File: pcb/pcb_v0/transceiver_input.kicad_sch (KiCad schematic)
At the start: 26 parts, among them U2 LM324

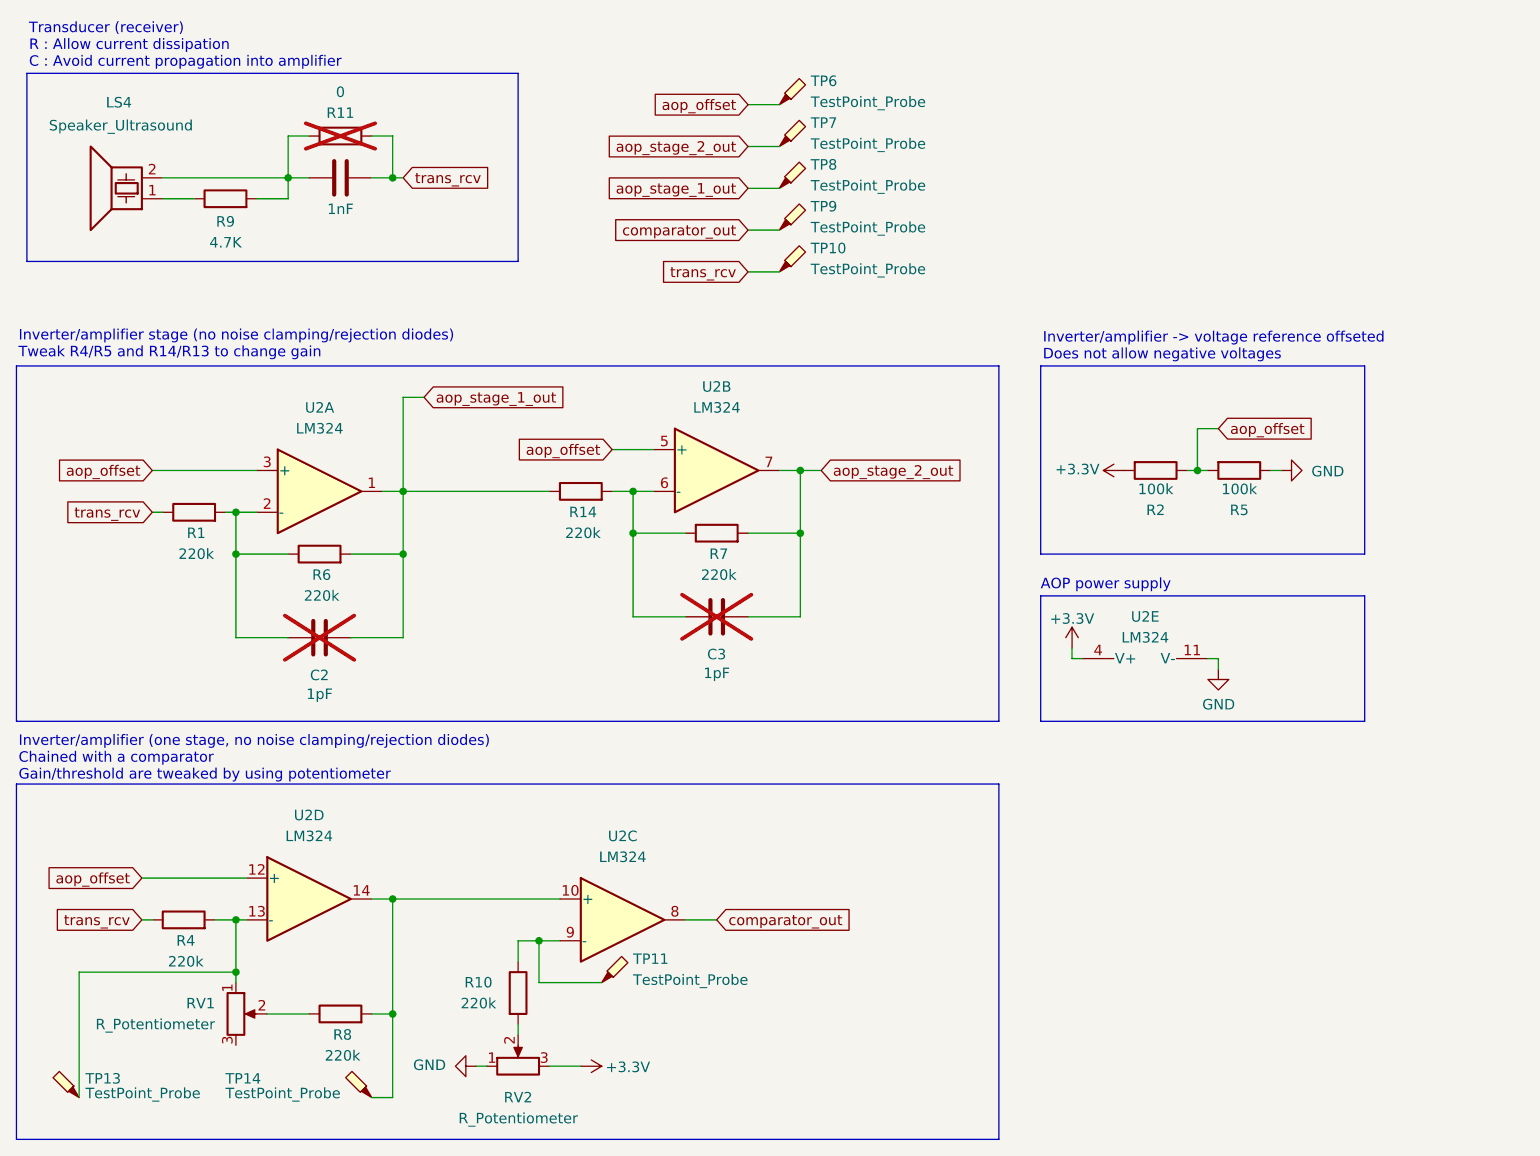
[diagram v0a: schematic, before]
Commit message: fix(pcb_v0): Update resistor and capacitor values
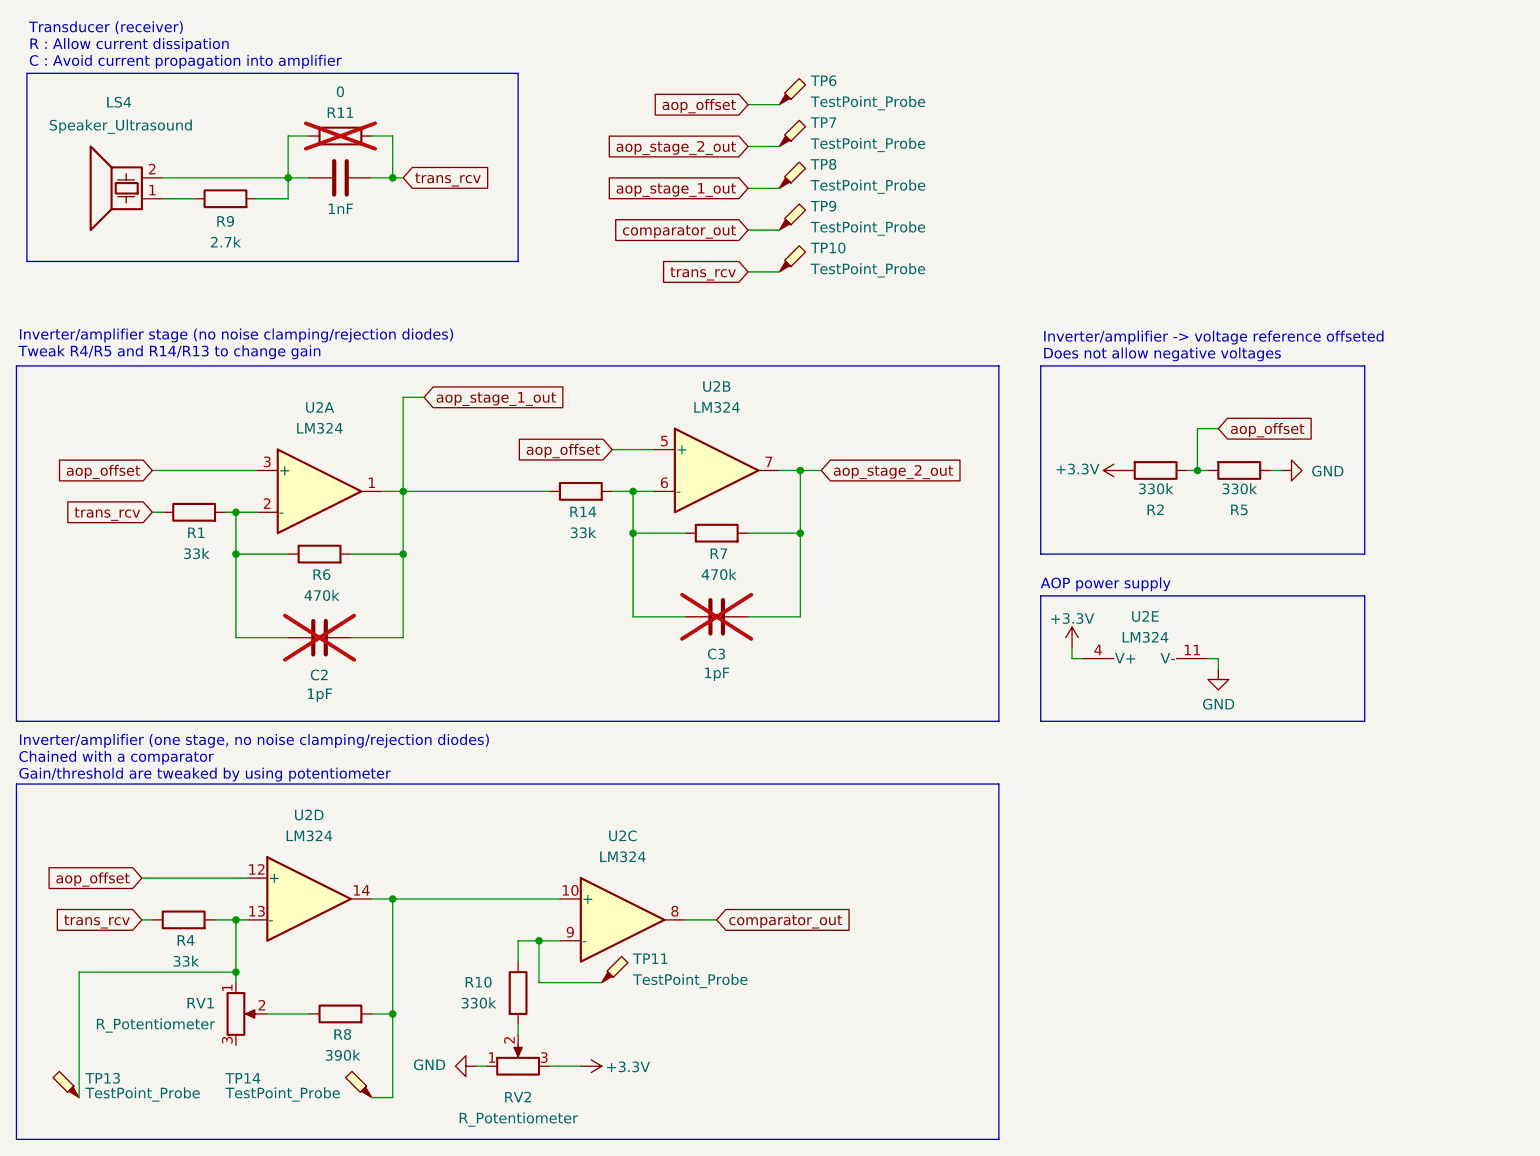
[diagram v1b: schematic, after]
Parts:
- R1, R14, R4: value 220k -> 33k
- R10: value 220k -> 330k
- R2, R5: value 100k -> 330k
- R6, R7: value 220k -> 470k
- R8: value 220k -> 390k
- R9: value 4.7K -> 2.7k
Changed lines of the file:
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@@
 			)
 		)
-		(property "Value" "220k"
+		(property "Value" "33k"
 			(at 68.834 92.71 90)
 			(effects
@@
 			)
 		)
-		(property "Value" "100k"
+		(property "Value" "330k"
 			(at 185.42 84.836 90)
 			(effects
@@
 			)
 		)
-		(property "Value" "220k"
+		(property "Value" "330k"
 			(at 103.124 147.32 0)
 			(effects
@@
 			)
 		)
-		(property "Value" "4.7K"
+		(property "Value" "2.7k"
 			(at 72.39 54.864 90)
 			(effects
@@
 			)
 		)
-		(property "Value" "100k"
+		(property "Value" "330k"
 			(at 195.58 84.836 90)
 			(effects
@@
 			)
 		)
-		(property "Value" "220k"
+		(property "Value" "470k"
 			(at 132.334 95.25 90)
 			(effects
@@
 			)
 		)
-		(property "Value" "220k"
+		(property "Value" "33k"
 			(at 67.564 142.24 90)
 			(effects
@@
 			)
 		)
-		(property "Value" "220k"
+		(property "Value" "33k"
 			(at 115.824 90.17 90)
 			(effects
@@
 			)
 		)
-		(property "Value" "220k"
+		(property "Value" "470k"
 			(at 84.074 97.79 90)
 			(effects
@@
 			)
 		)
-		(property "Value" "220k"
+		(property "Value" "390k"
 			(at 86.614 153.67 90)
 			(effects
